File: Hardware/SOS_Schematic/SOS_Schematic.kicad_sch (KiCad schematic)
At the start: 26 parts, among them J1 USB_B_Mini, J2 Conn_02x07_Odd_Even, U1 MCP1802x-xx02xOT, U2 STM32L476RGTx, U3 HTRC11001T, Y1 Crystal_Small

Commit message: power supply schematic
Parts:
- added C17, C18: 1u, symbol Device:C_Small
- U1: value MCP1802x-xx02xOT -> BU33SD5WG-TR
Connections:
- net +3.3V: now also U1.5 (VOUT), C18.1
- net GND: now also U1.2 (GND), C17.2, C18.2
- net +5V: now reaches U1.1 (VIN)
- net +5V: now also C17.1
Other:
- note added: "lié à Vin si toujours on, sinon interrupteur"
- moved on the sheet: U1

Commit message: schema pdf
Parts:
- added H1, H2, H3, H4: MountingHole_Pad, symbol Mechanical:MountingHole_Pad
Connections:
- net GND: now also H1.1, H2.1, H3.1, H4.1
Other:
- note added: "Mounting pad"
- moved on the sheet: C12, C13, L2

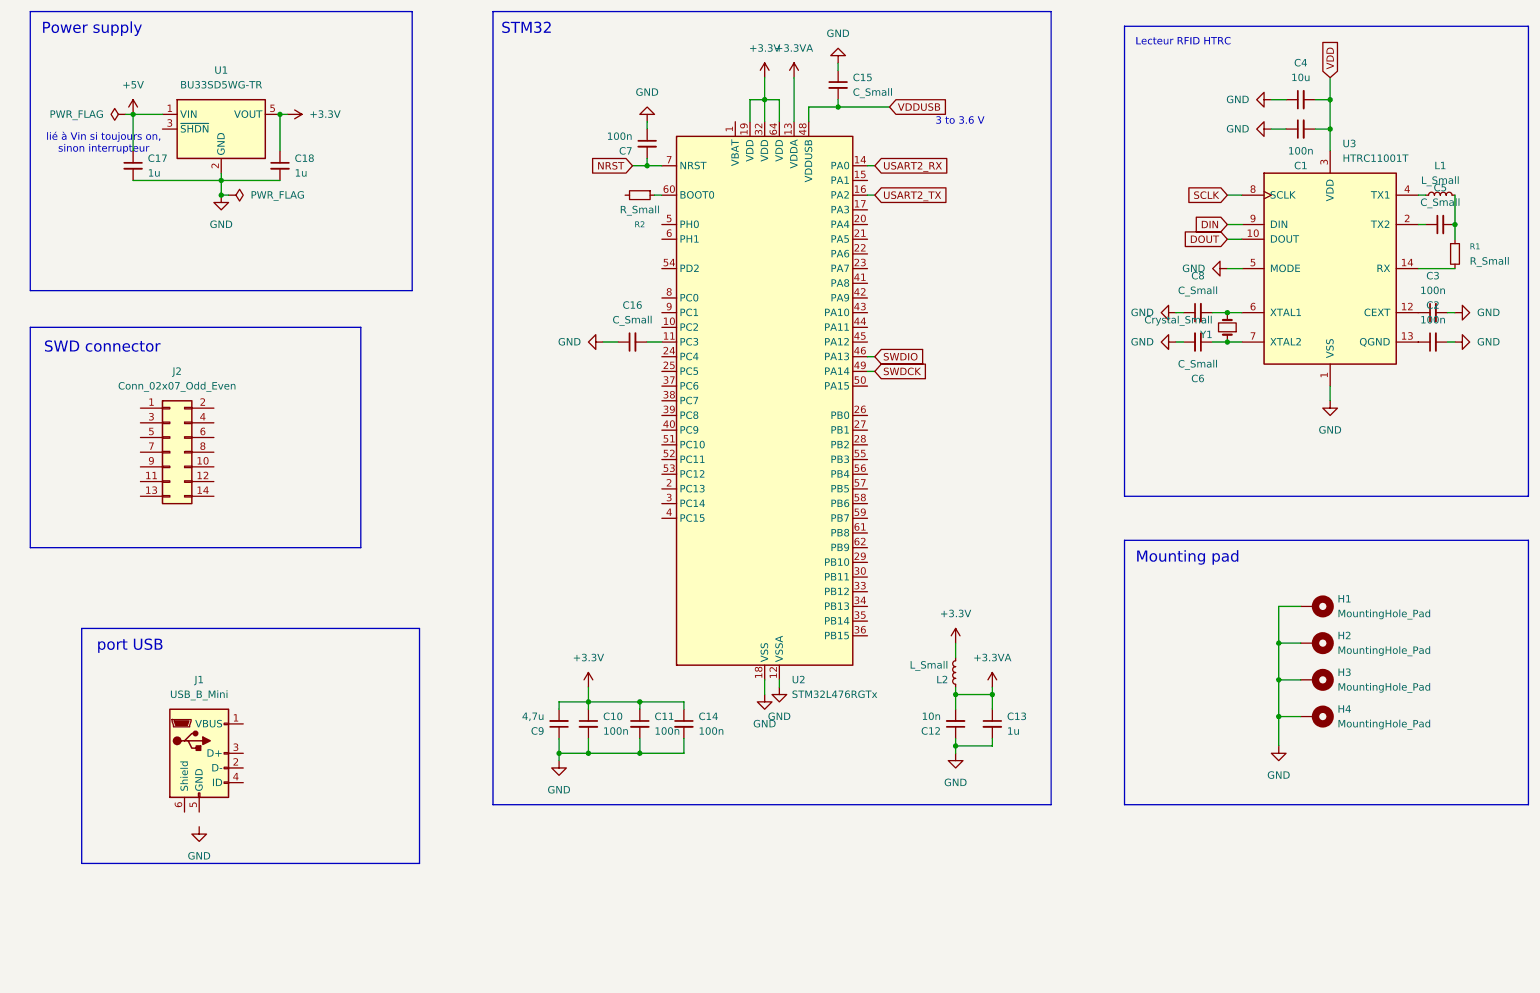
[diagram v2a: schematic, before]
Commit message: schematic basics (usb and  spec pins left)
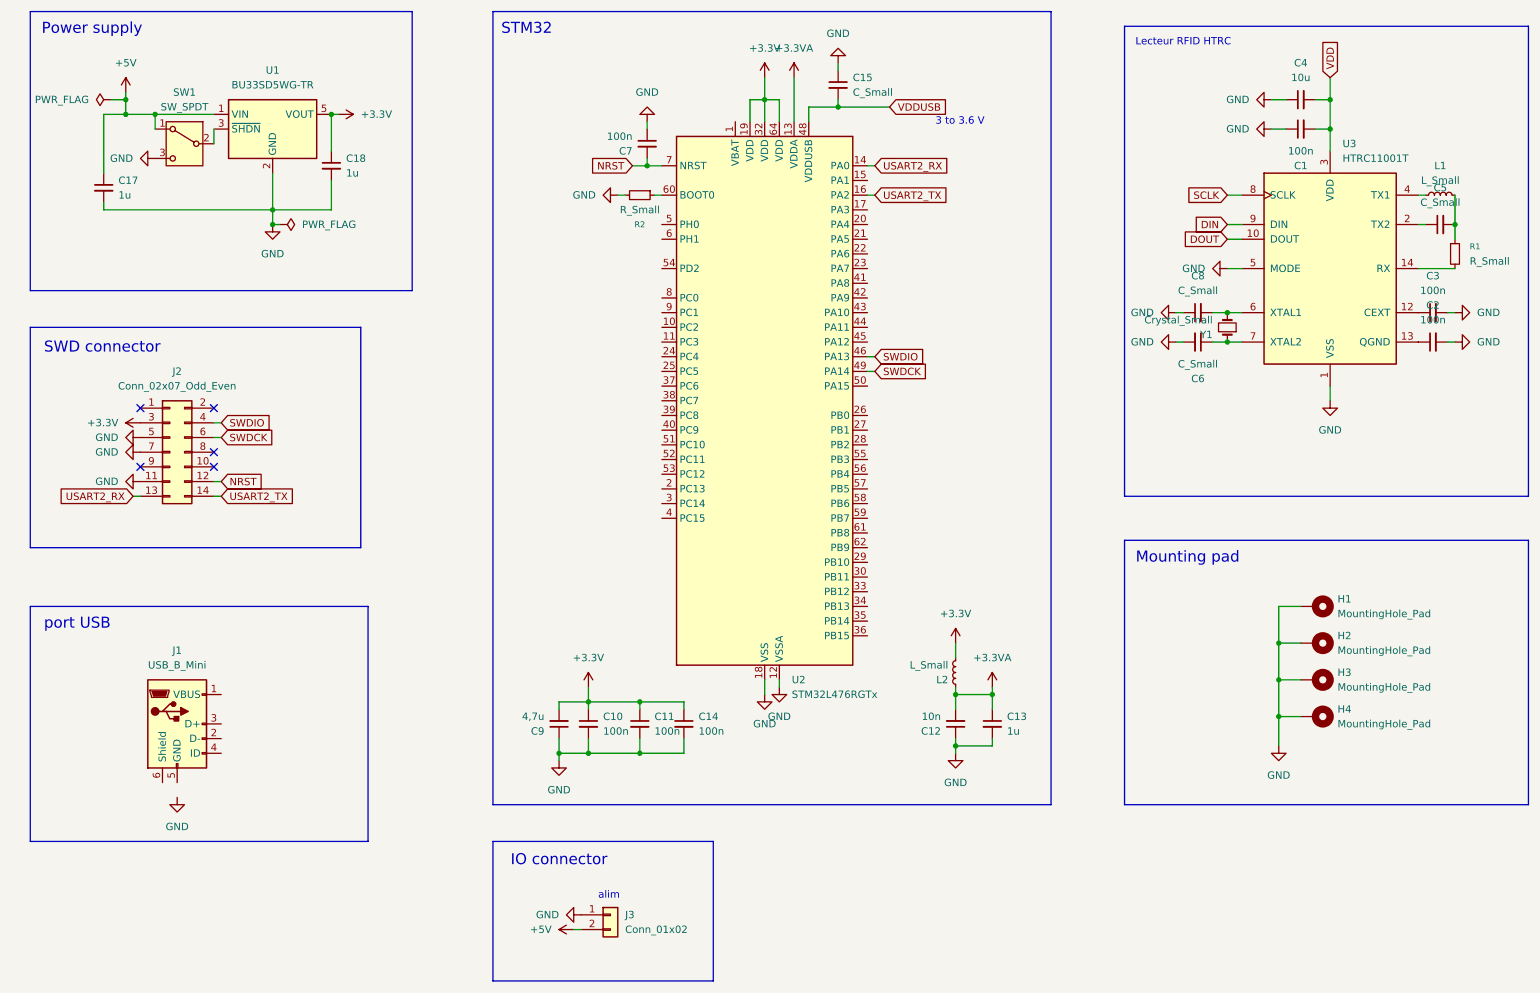
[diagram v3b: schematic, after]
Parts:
- removed C16: C_Small, symbol Device:C_Small
- added J3: Conn_01x02, symbol Connector_Generic:Conn_01x02
- added SW1: SW_SPDT, symbol Switch:SW_SPDT
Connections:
- net +3.3V: now also J2.3 (Pin_3)
- net +5V: now also J3.2 (Pin_2), SW1.1 (A)
- net GND: now also J2.11 (Pin_11), J2.5 (Pin_5), J2.7 (Pin_7), R2.2, J3.1 (Pin_1), SW1.3 (C)
- net NRST: now also J2.12 (Pin_12)
- net SWDCK: now also J2.6 (Pin_6)
- net SWDIO: now also J2.4 (Pin_4)
- net USART2_RX: now also J2.13 (Pin_13)
- net USART2_TX: now also J2.14 (Pin_14)
- net at U1.3 (~{SHDN}): now also SW1.2 (B)
- no-connect marks 0 -> 5
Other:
- note added: "IO connector"
- note added: "alim"
- note removed: "lié à Vin si toujours on, sinon interrupteur"
- moved on the sheet: C17, C18, J1, U1

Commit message: schematic pre-final version
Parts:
- added C16, C19: C_Small, symbol Device:C_Small
- added R3: 100K, symbol Device:R_Small
- added Y2: Crystal_Small, symbol Device:Crystal_Small
- C5: value C_Small -> 1,5n
- C6, C8: value C_Small -> 22p
- L1: value L_Small -> 1/2 uH
- R1: value R_Small -> 2,2k
- Y1: value Crystal_Small -> 13,56MHz
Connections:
- net DIN is gone; now on net SPI1_MOSI: U3.9 (DIN)
- net VDD is gone; now on net +3.3V: C1.2, C4.2, U3.3 (VDD)
- net +5V: now also J1.1 (VBUS)
- net GND: now also J1.5 (GND), J1.6 (Shield), R2.1, C16.1, C19.2, R3.2; no longer R2.2
- net USART2_RX: now also U2.17 (PA3); no longer U2.14 (PA0)
- net USBDM: now reaches J1.2 (D-)
- net USBDM: now also U2.44 (PA11)
- net USBDP: now reaches J1.3 (D+)
- net USBDP: now also U2.45 (PA12)
- net at J1.4 (ID): now also R3.1
- net at U2.60 (BOOT0): now also R2.2; no longer R2.1
- net SPI1_SCK: now reaches U2.21 (PA5)
- net SPI1_MISO: now reaches U2.22 (PA6)
- net SPI1_MOSI: now reaches U2.23 (PA7)
- net OSC_IN: now reaches U2.5 (PH0)
- net OSC_IN: now also C16.2, Y2.2
- net OSC_OUT: now reaches U2.6 (PH1)
- net OSC_OUT: now also C19.1, Y2.1
- net DOUT renamed SPIA_MISO
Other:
- moved on the sheet: R2

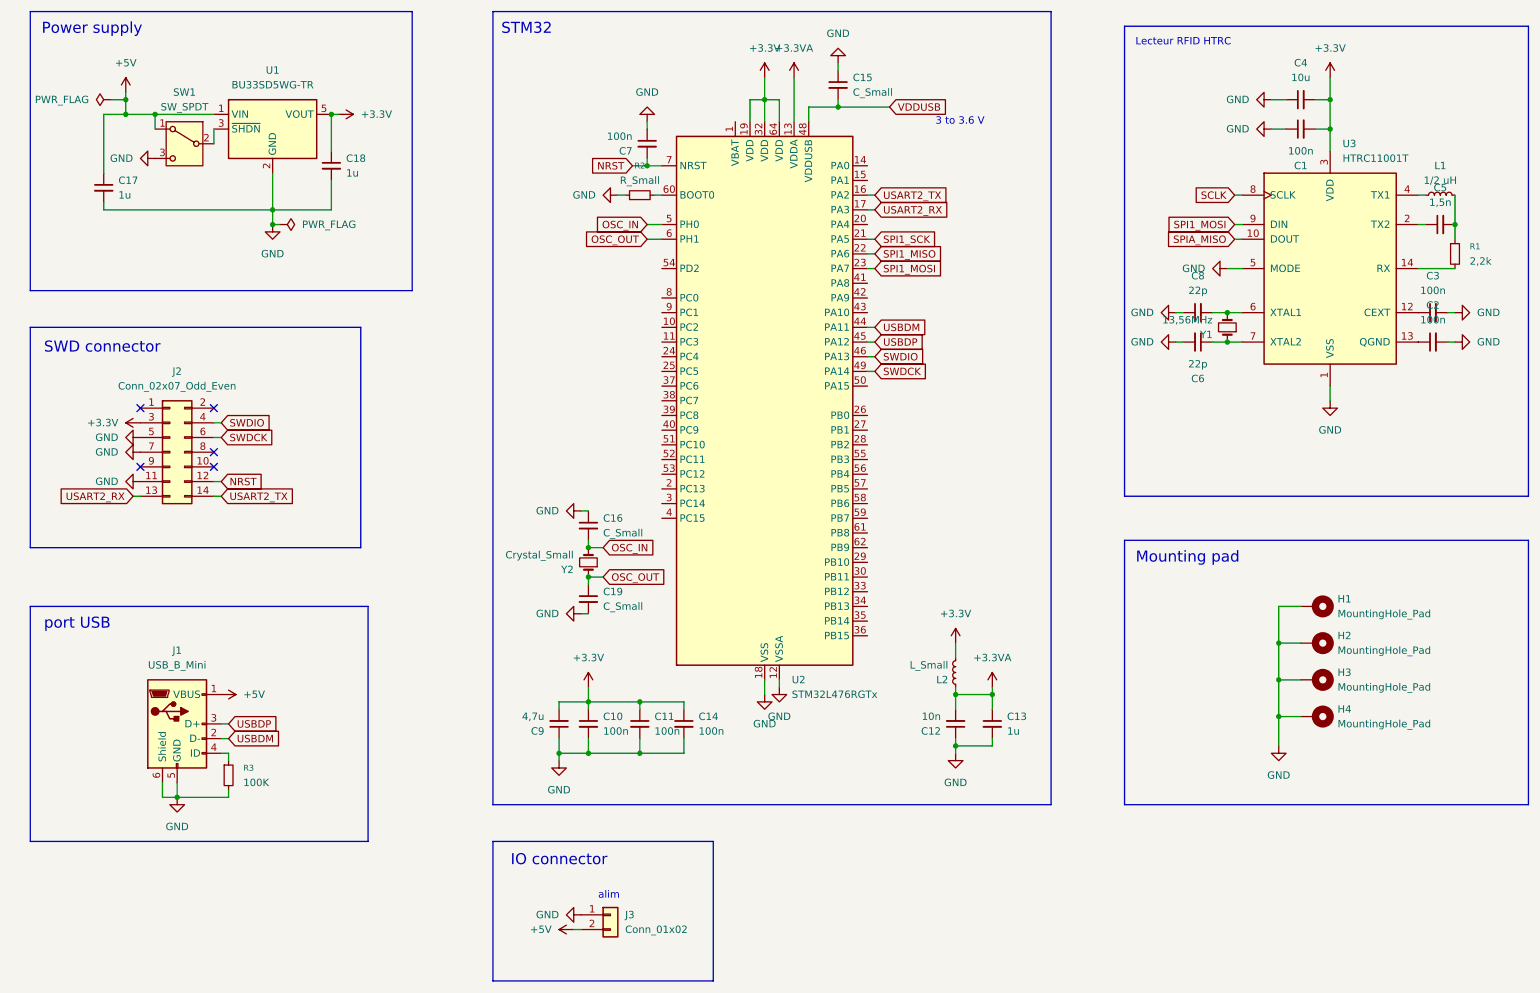
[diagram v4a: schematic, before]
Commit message: schematic post 1st revision (Vbat and SWD connector left)
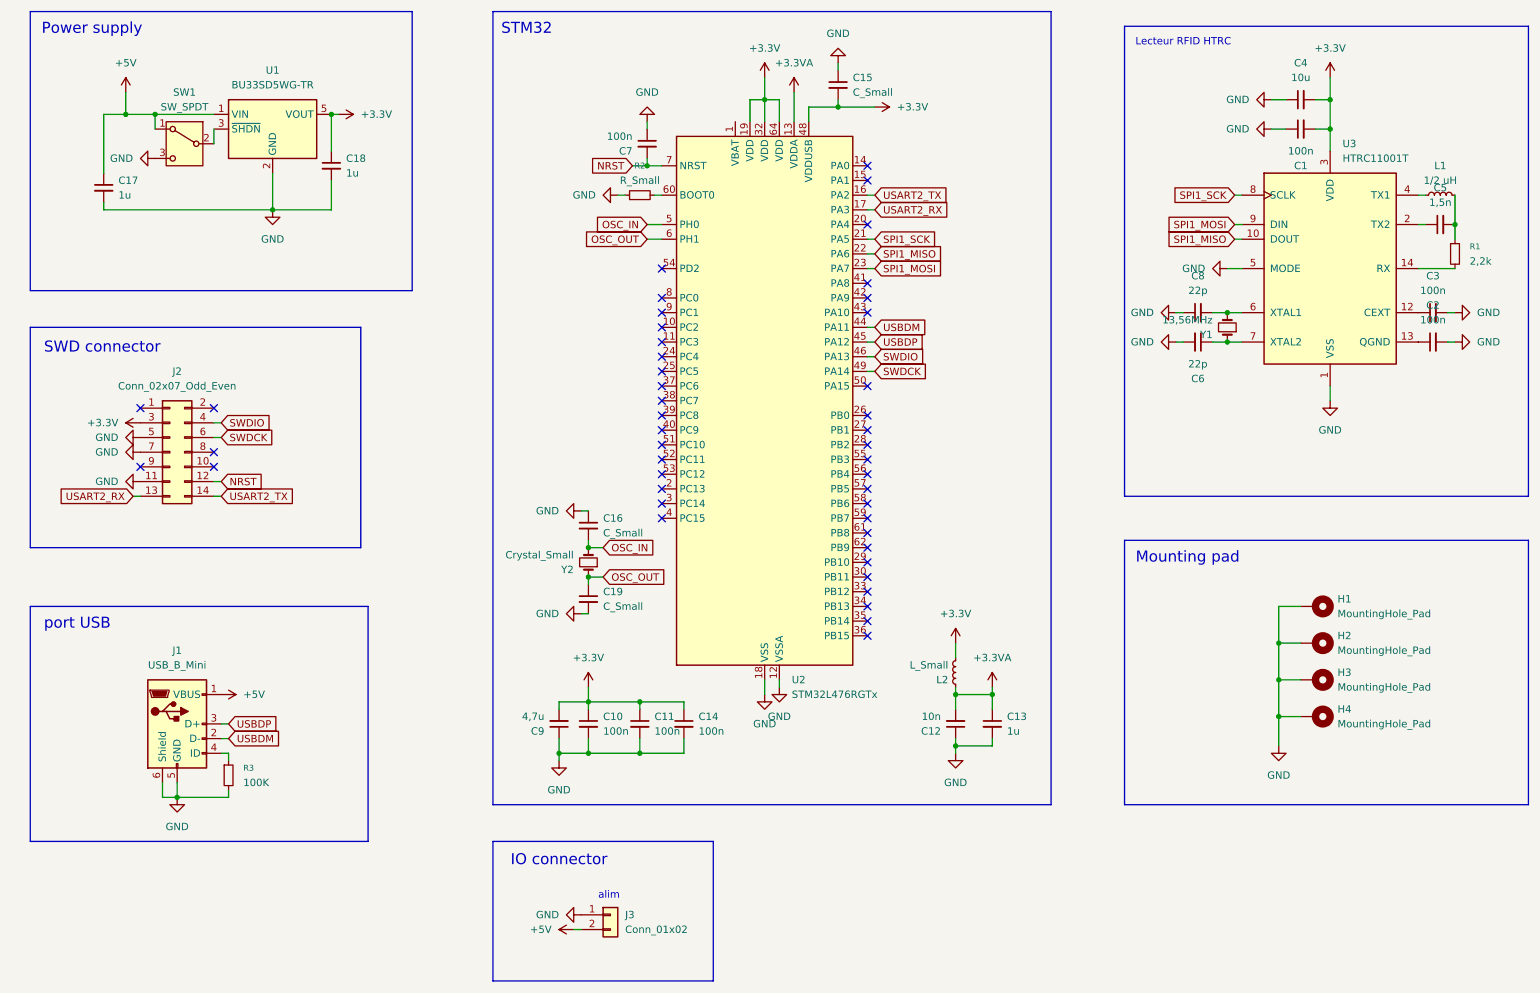
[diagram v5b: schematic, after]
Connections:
- net SCLK is gone; now on net SPI1_SCK: U3.8 (SCLK)
- net SPIA_MISO is gone; now on net SPI1_MISO: U3.10 (DOUT)
- net VDDUSB is gone; now on net +3.3V: C15.2, U2.48 (VDDUSB)
- no-connect marks 5 -> 45
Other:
- note removed: "3 to 3.6 V"

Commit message: final schematic
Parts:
- removed J2: Conn_02x07_Odd_Even, symbol Connector_Generic:Conn_02x07_Odd_Even
- added C20: 1u, symbol Device:C_Small
- added J2: Conn_02x10_Odd_Even, symbol Connector_Generic:Conn_02x10_Odd_Even
- added R4, R5, R6: 10k, symbol Device:R_Small
- added R7: 390, symbol Device:R_Small
- C15: value C_Small -> 100n
- C16, C19: value C_Small -> 20p
- R2: value R_Small -> 10k
- Y2: value Crystal_Small -> 8MHz
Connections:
- net +3.3V: now also U2.1 (VBAT), C20.1, J2.1 (Pin_1), J2.2 (Pin_2)
- net GND: now also C20.2, J2.10 (Pin_10), J2.12 (Pin_12), J2.14 (Pin_14), J2.16 (Pin_16), J2.18 (Pin_18), J2.20 (Pin_20), J2.4 (Pin_4), J2.6 (Pin_6), J2.8 (Pin_8), R4.1, R5.1, R6.2
- net NRST: now also J2.15 (Pin_15)
- net OSC_OUT: now also R7.1; no longer C19.1, Y2.1
- net SWDCK: now also J2.9 (Pin_9)
- net SWDIO: now also J2.7 (Pin_7)
- net TDI: now reaches U2.50 (PA15)
- net TDI: now also J2.5 (Pin_5)
- net TDO: now reaches U2.55 (PB3)
- net TDO: now also J2.13 (Pin_13)
- net TRST: now reaches U2.56 (PB4)
- net TRST: now also J2.3 (Pin_3)
- net USART2_RX: no longer names the net of U2.17 (PA3)
- net USART2_TX: no longer names the net of U2.16 (PA2)
- new net: C19.1, R7.2, Y2.1
- new net: J2.11 (Pin_11), R4.2
- new net: J2.17 (Pin_17), R5.2
- new net: J2.19 (Pin_19), R6.1
- no-connect marks 45 -> 39
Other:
- moved on the sheet: C15, C16, C19, C6, C7, C8, J1, R1, R3, Y2
